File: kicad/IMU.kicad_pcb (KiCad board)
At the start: 4 copper layers, 37.6 x 37.6 mm, 89 parts, among them IC1 FT232RQ, P1 M1P, P10 CONN_01X02, P11 CONN_02X05, P12 CONN_02X06, P2 M1N, P3 M3P, P4 M3N, P5 JTAG_DB, P6 M2P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

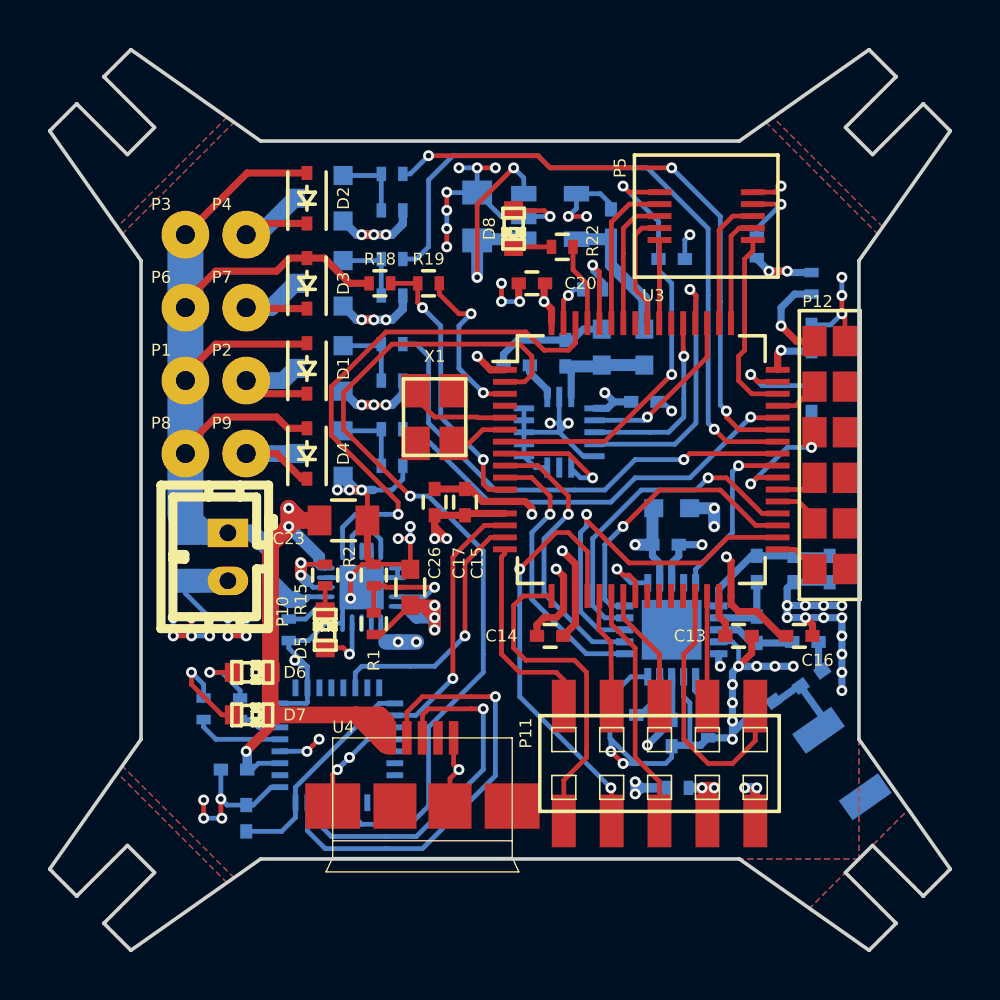
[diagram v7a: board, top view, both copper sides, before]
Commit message: Connect CS of MEMS to mcu.
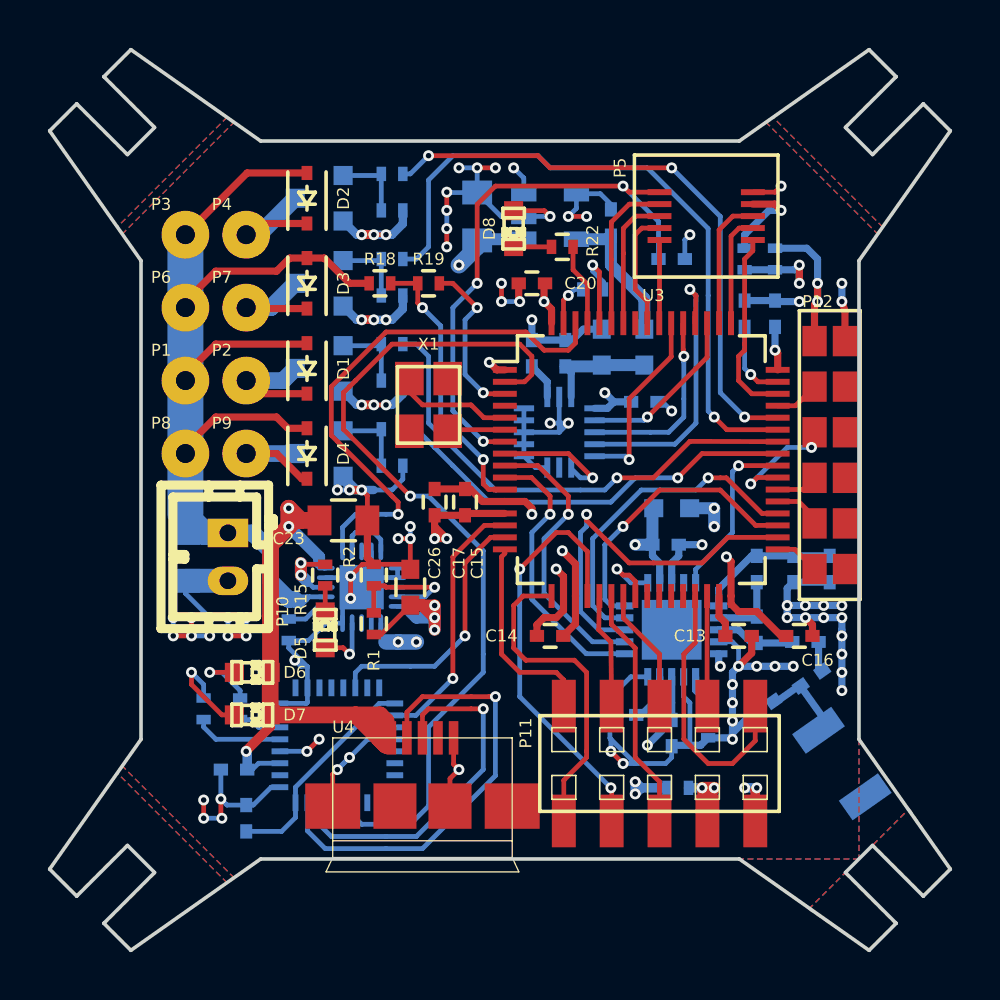
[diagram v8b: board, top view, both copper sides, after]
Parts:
- moved C12 4.52 mm to (125.2, 77.2), turned to 90 degrees
- moved C19 1.83 mm to (126.5, 77.2)
- moved R17 1.83 mm to (126.5, 74.9), turned to 90 degrees
- moved C1 0.81 mm to (116.3, 78.9), turned to 90 degrees
- moved R14 0.72 mm to (125.2, 74.9)
- moved X1 0.57 mm to (112.0, 81.0)
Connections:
- U1 pad 5: GND -> /Mems and Radio/MEMS_CS
- U3 pad 41: /Microcontroller/M1 -> /Microcontroller/M4
- U3 pad 42: /Microcontroller/M2 -> /Microcontroller/M1
- U3 pad 43: /Microcontroller/M3 -> /Microcontroller/M2
- U3 pad 44: /Microcontroller/M4 -> /Microcontroller/M3
- U3 pad 54: Net-(U3-Pad54) -> /Mems and Radio/MEMS_CS
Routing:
- net /Mems and Radio/MEMS_CS: track 0.00 -> 7.93 mm, vias 0 -> 1
- net /Microcontroller/NRST: track 18.5 -> 23.5 mm, vias 2 -> 3
- net GND: track 161.9 -> 159.6 mm, vias 86 -> 87
- net Net-(P12-Pad1): track 3.93 -> 6.21 mm, vias 1 -> 2
- net Net-(P5-Pad4): track 2.93 -> 3.80 mm
- net /Microcontroller/M3: track 25.5 -> 24.8 mm
- net /Microcontroller/M4: track 18.4 -> 17.8 mm
- net Net-(C12-Pad1): track 3.99 -> 3.35 mm
- net Net-(U3-Pad5): track 4.38 -> 4.99 mm
- net /Microcontroller/M2: track 28.8 -> 28.3 mm
